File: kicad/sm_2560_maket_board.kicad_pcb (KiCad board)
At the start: 2 copper layers, 81.8 x 61.7 mm, 503 parts

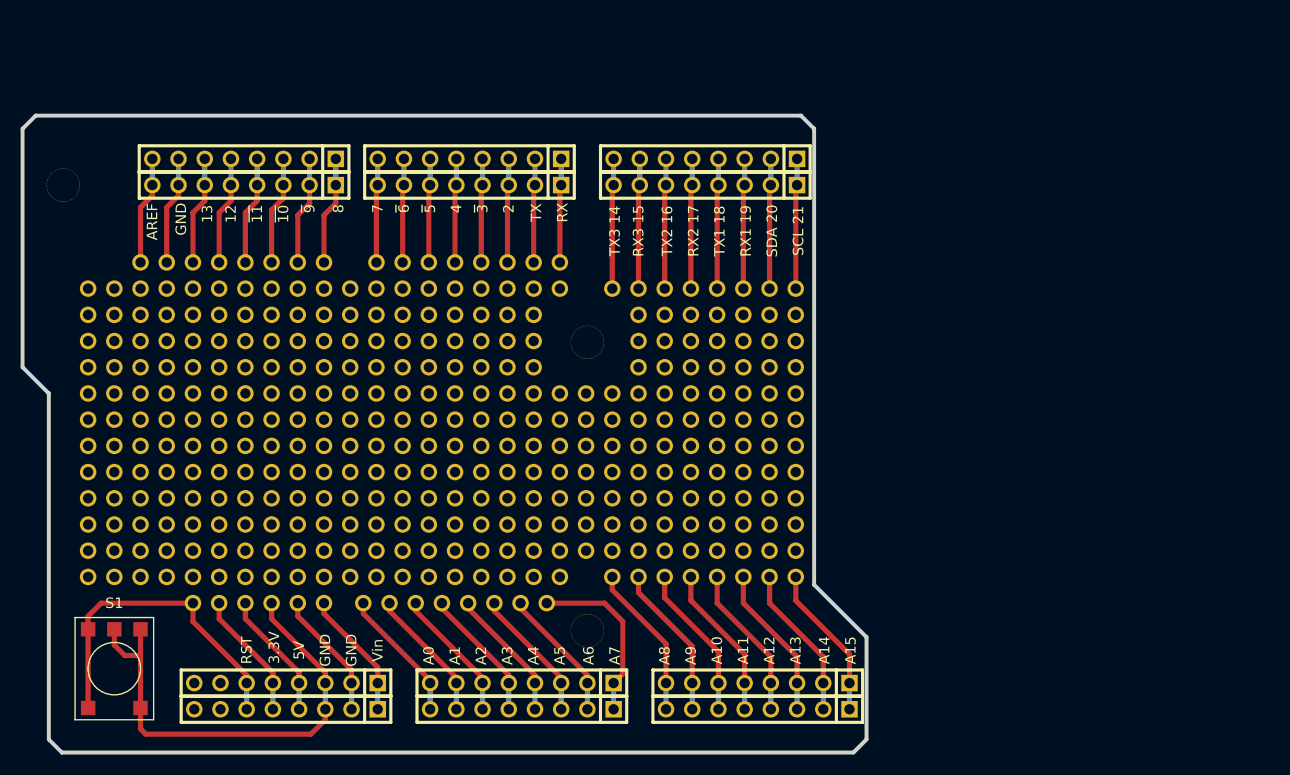
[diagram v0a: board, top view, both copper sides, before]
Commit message: Поправил макетное поле под новую версию платы SafeDuino 2560 ver 2.0.
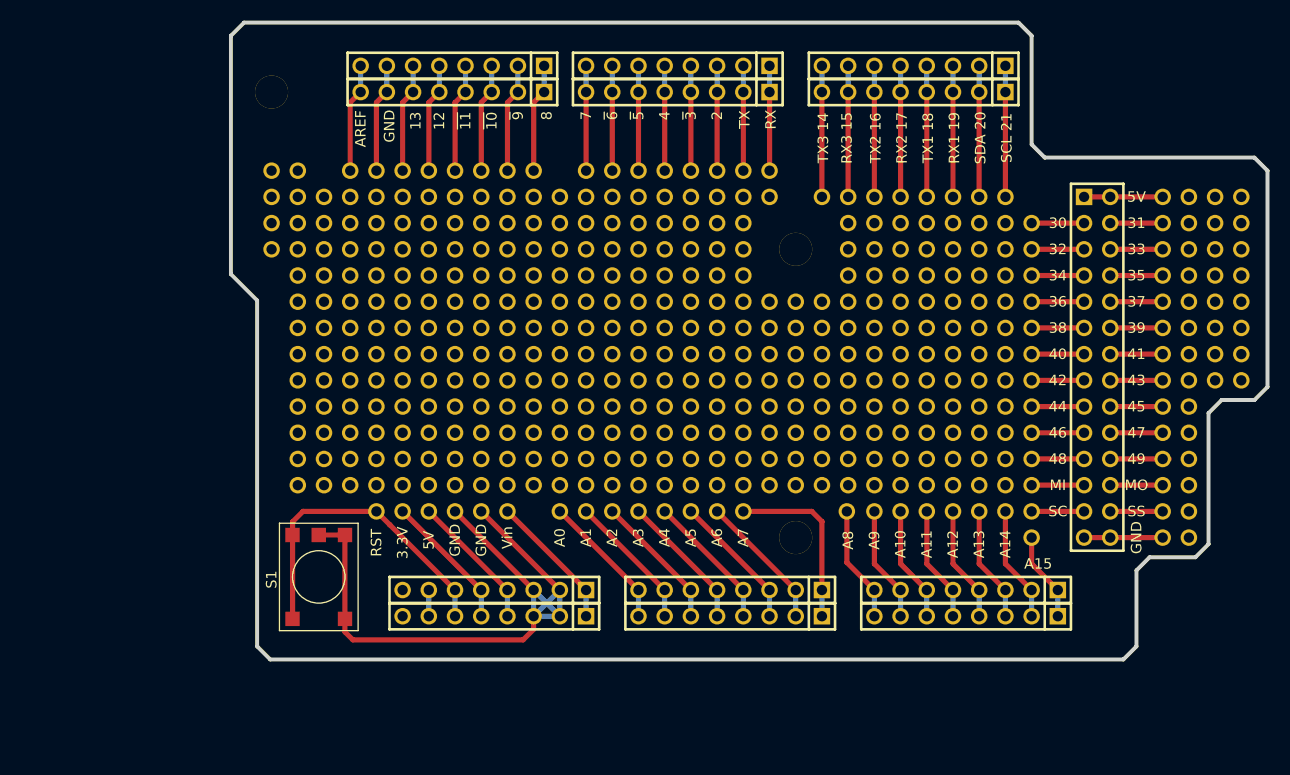
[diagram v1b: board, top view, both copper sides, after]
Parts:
- removed the arduino at (97.9, 136.5)
- removed the arduino at (106.7, 134.6)
- removed the arduino at (83.8, 111.8)
- removed the arduino at (81.7, 112.4)
- removed the arduino at (86.4, 111.8)
- removed the arduino at (94.0, 111.8)
- removed the arduino at (89.3, 112.4)
- removed the arduino at (91.4, 111.8)
- removed the arduino at (88.9, 111.8)
- removed the arduino at (112.1, 112.4)
- removed the arduino at (114.3, 111.8)
- removed the arduino at (111.8, 111.8)
- removed the arduino at (104.5, 135.3)
- removed the arduino at (112.1, 111.1) (x2)
- removed the arduino at (112.1, 108.6) (x2)
- removed the arduino at (111.8, 109.2)
- removed the arduino at (114.3, 109.2)
- removed the arduino at (112.1, 109.9)
- removed the arduino at (88.9, 109.2)
- removed the arduino at (91.4, 109.2)
- removed the arduino at (89.3, 109.9)
- removed the arduino at (94.0, 109.2)
- removed the arduino at (86.4, 109.2)
- removed the arduino at (109.2, 134.6)
- removed the arduino at (81.7, 109.9)
- removed the arduino at (83.8, 109.2)
- removed the arduino at (81.3, 109.2)
- removed the arduino at (96.5, 109.2)
- removed the arduino at (99.1, 109.2)
- removed the arduino at (96.9, 109.9)
- removed the arduino at (101.6, 109.2)
- removed the arduino at (109.2, 109.2)
- removed the arduino at (104.5, 109.9)
- removed the arduino at (106.7, 109.2)
- removed the arduino at (101.6, 134.6)
- removed the arduino at (104.1, 109.2)
- removed the arduino at (79.1, 109.9)
- removed the arduino at (78.7, 109.2)
- removed the arduino at (76.2, 109.2)
- removed the arduino at (71.5, 109.9)
- removed the arduino at (73.7, 109.2)
- removed the arduino at (71.1, 109.2)
- removed the arduino at (71.1, 114.3)
- removed the arduino at (73.7, 114.3)
- removed the arduino at (96.9, 135.3)
- removed the arduino at (71.5, 114.9)
- removed the arduino at (76.2, 114.3)
- removed the arduino at (78.7, 114.3)
- removed the arduino at (79.1, 114.9)
- removed the arduino at (104.1, 114.3)
- removed the arduino at (106.7, 114.3)
- removed the arduino at (104.5, 114.9)
- removed the arduino at (109.2, 114.3)
- removed the arduino at (101.6, 114.3)
- removed the arduino at (96.9, 114.9)
- removed the arduino at (99.1, 134.6)
- removed the arduino at (99.1, 114.3)
- removed the arduino at (96.5, 114.3)
- removed the arduino at (81.3, 114.3)
- removed the arduino at (83.8, 114.3)
- removed the arduino at (81.7, 114.9)
- removed the arduino at (86.4, 114.3)
- removed the arduino at (94.0, 114.3)
- removed the arduino at (89.3, 114.9)
- removed the arduino at (91.4, 114.3)
- removed the arduino at (88.9, 114.3)
- removed the arduino at (96.5, 134.6)
- removed the arduino at (112.1, 114.9)
- removed the arduino at (114.3, 114.3)
- removed the arduino at (111.8, 114.3)
- removed the arduino at (112.1, 113.7)
- removed the arduino at (112.1, 116.2)
- removed the arduino at (134.6, 124.5)
- removed the arduino at (137.2, 124.5)
- removed the arduino at (135.0, 125.1)
- removed the arduino at (139.7, 124.5)
- removed the arduino at (132.1, 124.5)
- removed the arduino at (81.3, 134.6)
- removed the arduino at (127.4, 125.1)
- removed the arduino at (129.5, 124.5)
- removed the arduino at (127.0, 124.5)
- removed the arduino at (111.8, 124.5)
- removed the arduino at (114.3, 124.5)
- removed the arduino at (112.1, 125.1)
- removed the arduino at (116.8, 124.5)
- removed the arduino at (124.5, 124.5)
- removed the arduino at (119.8, 125.1)
- removed the arduino at (121.9, 124.5)
- removed the arduino at (83.8, 134.6)
- removed the arduino at (119.4, 124.5)
- removed the arduino at (88.9, 124.5)
- removed the arduino at (91.4, 124.5)
- removed the arduino at (89.3, 125.1)
- removed the arduino at (94.0, 124.5)
- removed the arduino at (86.4, 124.5)
- removed the arduino at (81.7, 125.1)
- removed the arduino at (83.8, 124.5)
- removed the arduino at (81.3, 124.5)
- removed the arduino at (96.5, 124.5)
- removed the arduino at (81.7, 135.3)
- removed the arduino at (99.1, 124.5)
- removed the arduino at (96.9, 125.1)
- removed the arduino at (101.6, 124.5)
- removed the arduino at (109.2, 124.5)
- removed the arduino at (104.5, 125.1)
- removed the arduino at (106.7, 124.5)
- removed the arduino at (104.1, 124.5)
- removed the arduino at (79.1, 125.1)
- removed the arduino at (78.7, 124.5)
- removed the arduino at (76.2, 124.5)
- removed the arduino at (76.3, 136.5)
- removed the arduino at (86.4, 134.6)
- removed the arduino at (71.5, 125.1)
- removed the arduino at (73.7, 124.5)
- removed the arduino at (71.1, 124.5)
- removed the arduino at (71.1, 121.9)
- removed the arduino at (73.7, 121.9)
- removed the arduino at (71.5, 122.6)
- removed the arduino at (76.2, 121.9)
- removed the arduino at (78.7, 121.9)
- removed the arduino at (79.1, 122.6)
- removed the arduino at (104.1, 121.9)
- removed the arduino at (94.0, 134.6)
- removed the arduino at (106.7, 121.9)
- removed the arduino at (104.5, 122.6)
- removed the arduino at (109.2, 121.9)
- removed the arduino at (101.6, 121.9)
- removed the arduino at (96.9, 122.6)
- removed the arduino at (99.1, 121.9)
- removed the arduino at (96.5, 121.9)
- removed the arduino at (81.3, 121.9)
- removed the arduino at (83.8, 121.9)
- removed the arduino at (81.7, 122.6)
- removed the arduino at (89.3, 135.3)
- removed the arduino at (86.4, 121.9)
- removed the arduino at (94.0, 121.9)
- removed the arduino at (89.3, 122.6)
- removed the arduino at (91.4, 121.9)
- removed the arduino at (88.9, 121.9)
- removed the arduino at (119.4, 121.9)
- removed the arduino at (121.9, 121.9)
- removed the arduino at (119.8, 122.6)
- removed the arduino at (124.5, 121.9)
- removed the arduino at (116.8, 121.9)
- removed the arduino at (91.4, 134.6)
- removed the arduino at (112.1, 122.6)
- removed the arduino at (114.3, 121.9)
- removed the arduino at (111.8, 121.9)
- removed the arduino at (127.0, 121.9)
- removed the arduino at (129.5, 121.9)
- removed the arduino at (127.4, 122.6)
- removed the arduino at (132.1, 121.9)
- removed the arduino at (139.7, 121.9)
- removed the arduino at (135.0, 122.6)
- removed the arduino at (137.2, 121.9)
- removed the arduino at (88.9, 134.6)
- removed the arduino at (134.6, 121.9)
- removed the arduino at (134.6, 116.8)
- removed the arduino at (137.2, 116.8)
- removed the arduino at (135.0, 117.5)
- removed the arduino at (139.7, 116.8)
- removed the arduino at (132.1, 116.8)
- removed the arduino at (127.4, 117.5)
- removed the arduino at (129.5, 116.8)
- removed the arduino at (127.0, 116.8)
- removed the arduino at (111.8, 116.8)
- removed the arduino at (116.8, 134.6)
- removed the arduino at (114.3, 116.8)
- removed the arduino at (112.1, 117.5)
- removed the arduino at (116.8, 116.8)
- removed the arduino at (124.5, 116.8)
- removed the arduino at (119.8, 117.5)
- removed the arduino at (121.9, 116.8)
- removed the arduino at (119.4, 116.8)
- removed the arduino at (88.9, 116.8)
- removed the arduino at (91.4, 116.8)
- removed the arduino at (89.3, 117.5)
- removed the arduino at (112.1, 135.3)
- removed the arduino at (94.0, 116.8)
- removed the arduino at (86.4, 116.8)
- removed the arduino at (81.7, 117.5)
- removed the arduino at (83.8, 116.8)
- removed the arduino at (81.3, 116.8)
- removed the arduino at (96.5, 116.8)
- removed the arduino at (99.1, 116.8)
- removed the arduino at (96.9, 117.5)
- removed the arduino at (101.6, 116.8)
- removed the arduino at (109.2, 116.8)
- removed the arduino at (114.3, 134.6)
- removed the arduino at (104.5, 117.5)
- removed the arduino at (106.7, 116.8)
- removed the arduino at (104.1, 116.8)
- removed the arduino at (79.1, 117.5)
- removed the arduino at (78.7, 116.8)
- removed the arduino at (76.2, 116.8)
- removed the arduino at (71.5, 117.5)
- removed the arduino at (73.7, 116.8)
- removed the arduino at (71.1, 116.8)
- removed the arduino at (71.1, 119.4)
- removed the arduino at (111.8, 134.6)
- removed the arduino at (73.7, 119.4)
- removed the arduino at (71.5, 120.0)
- removed the arduino at (76.2, 119.4)
- removed the arduino at (78.7, 119.4)
- removed the arduino at (79.1, 120.0)
- removed the arduino at (104.1, 119.4)
- removed the arduino at (106.7, 119.4)
- removed the arduino at (104.5, 120.0)
- removed the arduino at (109.2, 119.4)
- removed the arduino at (101.6, 119.4)
- removed the arduino at (116.8, 106.7)
- removed the arduino at (96.9, 120.0)
- removed the arduino at (99.1, 119.4)
- removed the arduino at (96.5, 119.4)
- removed the arduino at (81.3, 119.4)
- removed the arduino at (83.8, 119.4)
- removed the arduino at (81.7, 120.0)
- removed the arduino at (86.4, 119.4)
- removed the arduino at (94.0, 119.4)
- removed the arduino at (89.3, 120.0)
- removed the arduino at (91.4, 119.4)
- removed the arduino at (71.1, 134.6)
- removed the arduino at (112.1, 106.0) (x3)
- removed the arduino at (88.9, 119.4)
- removed the arduino at (119.4, 119.4)
- removed the arduino at (121.9, 119.4)
- removed the arduino at (119.8, 120.0)
- removed the arduino at (124.5, 119.4)
- removed the arduino at (116.8, 119.4)
- removed the arduino at (112.1, 120.0)
- removed the arduino at (114.3, 119.4)
- removed the arduino at (111.8, 119.4)
- removed the arduino at (127.0, 119.4)
- removed the arduino at (71.1, 106.7)
- removed the arduino at (129.5, 119.4)
- removed the arduino at (127.4, 120.0)
- removed the arduino at (132.1, 119.4)
- removed the arduino at (139.7, 119.4)
- removed the arduino at (135.0, 120.0)
- removed the arduino at (137.2, 119.4)
- removed the arduino at (134.6, 119.4)
- removed the arduino at (112.1, 121.3)
- removed the arduino at (134.6, 129.5)
- removed the arduino at (73.7, 106.7)
- removed the arduino at (137.2, 129.5)
- removed the arduino at (135.0, 130.2)
- removed the arduino at (139.7, 129.5)
- removed the arduino at (132.1, 129.5)
- removed the arduino at (127.4, 130.2)
- removed the arduino at (129.5, 129.5)
- removed the arduino at (127.0, 129.5)
- removed the arduino at (111.8, 129.5)
- removed the arduino at (114.3, 129.5)
- removed the arduino at (112.1, 130.2)
- removed the arduino at (71.5, 107.3)
- removed the arduino at (116.8, 129.5)
- removed the arduino at (124.5, 129.5)
- removed the arduino at (119.8, 130.2)
- removed the arduino at (121.9, 129.5)
- removed the arduino at (119.4, 129.5)
- removed the arduino at (88.9, 129.5)
- removed the arduino at (91.4, 129.5)
- removed the arduino at (89.3, 130.2)
- removed the arduino at (94.0, 129.5)
- removed the arduino at (86.4, 129.5)
- removed the arduino at (76.2, 106.7)
- removed the arduino at (81.7, 130.2)
- removed the arduino at (83.8, 129.5)
- removed the arduino at (81.3, 129.5)
- removed the arduino at (96.5, 129.5)
- removed the arduino at (99.1, 129.5)
- removed the arduino at (96.9, 130.2)
- removed the arduino at (101.6, 129.5)
- removed the arduino at (109.2, 129.5)
- removed the arduino at (104.5, 130.2)
- removed the arduino at (106.7, 129.5)
- removed the arduino at (78.7, 106.7)
- removed the arduino at (104.1, 129.5)
- removed the arduino at (79.1, 130.2)
- removed the arduino at (78.7, 129.5)
- removed the arduino at (76.2, 129.5)
- removed the arduino at (71.5, 130.2)
- removed the arduino at (73.7, 129.5)
- removed the arduino at (71.1, 129.5)
- removed the arduino at (71.1, 127.0)
- removed the arduino at (73.7, 127.0)
- removed the arduino at (71.5, 127.6)
- removed the arduino at (79.1, 107.3)
- removed the arduino at (76.2, 127.0)
- removed the arduino at (78.7, 127.0)
- removed the arduino at (79.1, 127.6)
- removed the arduino at (104.1, 127.0)
- removed the arduino at (106.7, 127.0)
- removed the arduino at (104.5, 127.6)
- removed the arduino at (109.2, 127.0)
- removed the arduino at (101.6, 127.0)
- removed the arduino at (96.9, 127.6)
- removed the arduino at (99.1, 127.0)
- removed the arduino at (104.1, 106.7)
- removed the arduino at (96.5, 127.0)
- removed the arduino at (81.3, 127.0)
- removed the arduino at (83.8, 127.0)
- removed the arduino at (81.7, 127.6)
- removed the arduino at (86.4, 127.0)
- removed the arduino at (94.0, 127.0)
- removed the arduino at (89.3, 127.6)
- removed the arduino at (91.4, 127.0)
- removed the arduino at (88.9, 127.0)
- removed the arduino at (119.4, 127.0)
- removed the arduino at (106.7, 106.7)
- removed the arduino at (121.9, 127.0)
- removed the arduino at (119.8, 127.6)
- removed the arduino at (124.5, 127.0)
- removed the arduino at (116.8, 127.0)
- removed the arduino at (112.1, 127.6)
- removed the arduino at (114.3, 127.0)
- removed the arduino at (111.8, 127.0)
- removed the arduino at (127.0, 127.0)
- removed the arduino at (129.5, 127.0)
- removed the arduino at (127.4, 127.6)
- removed the arduino at (104.5, 107.3)
- removed the arduino at (132.1, 127.0)
- removed the arduino at (139.7, 127.0)
- removed the arduino at (135.0, 127.6)
- removed the arduino at (137.2, 127.0)
- removed the arduino at (134.6, 127.0)
- removed the arduino at (134.6, 132.1)
- removed the arduino at (137.2, 132.1)
- removed the arduino at (135.0, 132.7)
- removed the arduino at (139.7, 132.1)
- removed the arduino at (132.1, 132.1)
- removed the arduino at (73.7, 134.6)
- removed the arduino at (109.2, 106.7)
- removed the arduino at (127.4, 132.7)
- removed the arduino at (129.5, 132.1)
- removed the arduino at (127.0, 132.1)
- removed the arduino at (111.8, 132.1)
- removed the arduino at (114.3, 132.1)
- removed the arduino at (112.1, 132.7)
- removed the arduino at (116.8, 132.1)
- removed the arduino at (124.5, 132.1)
- removed the arduino at (119.8, 132.7)
- removed the arduino at (121.9, 132.1)
- removed the arduino at (101.6, 106.7)
- removed the arduino at (119.4, 132.1)
- removed the arduino at (88.9, 132.1)
- removed the arduino at (91.4, 132.1)
- removed the arduino at (89.3, 132.7)
- removed the arduino at (94.0, 132.1)
- removed the arduino at (86.4, 132.1)
- removed the arduino at (81.7, 132.7)
- removed the arduino at (83.8, 132.1)
- removed the arduino at (81.3, 132.1)
- removed the arduino at (96.5, 132.1)
- removed the arduino at (96.9, 107.3)
- removed the arduino at (99.1, 132.1)
- removed the arduino at (96.9, 132.7)
- removed the arduino at (101.6, 132.1)
- removed the arduino at (109.2, 132.1)
- removed the arduino at (104.5, 132.7)
- removed the arduino at (106.7, 132.1)
- removed the arduino at (104.1, 132.1)
- removed the arduino at (79.1, 132.7)
- removed the arduino at (78.7, 132.1)
- removed the arduino at (76.2, 132.1)
- removed the arduino at (99.1, 106.7)
- removed the arduino at (71.5, 132.7)
- removed the arduino at (73.7, 132.1)
- removed the arduino at (71.1, 132.1)
- removed the arduino at (76.2, 104.1)
- removed the arduino at (121.0, 106.0)
- removed the arduino at (139.7, 106.7)
- removed the arduino at (137.2, 106.7)
- removed the arduino at (132.1, 106.7)
- removed the arduino at (134.6, 106.7)
- removed the arduino at (124.5, 106.7)
- removed the arduino at (96.5, 106.7)
- removed the arduino at (121.9, 106.7)
- removed the arduino at (127.0, 106.7)
- removed the arduino at (129.5, 106.7)
- removed the arduino at (106.7, 104.1)
- removed the arduino at (104.1, 104.1)
- removed the arduino at (99.1, 104.1)
- removed the arduino at (101.6, 104.1)
- removed the arduino at (111.8, 104.1)
- removed the arduino at (109.2, 104.1)
- removed the arduino at (114.3, 104.1)
- removed the arduino at (81.3, 106.7)
- removed the arduino at (116.8, 104.1)
- removed the arduino at (98.2, 106.0)
- removed the arduino at (67.7, 118.7)
- removed the arduino at (94.0, 104.1)
- removed the arduino at (91.4, 104.1)
- removed the arduino at (86.4, 104.1)
- removed the arduino at (88.9, 104.1)
- removed the arduino at (78.7, 104.1)
- removed the arduino at (76.6, 106.0)
- removed the arduino at (81.3, 104.1)
- removed the arduino at (83.8, 106.7)
- removed the arduino at (83.8, 104.1)
- removed the arduino at (83.8, 137.2)
- removed the arduino at (81.3, 137.2)
- removed the arduino at (76.3, 134.0)
- removed the arduino at (88.9, 137.2)
- removed the arduino at (86.4, 137.2)
- removed the arduino at (91.4, 137.2)
- removed the arduino at (94.0, 137.2)
- removed the arduino at (75.1, 136.5)
- removed the arduino at (97.9, 134.0)
- removed the arduino at (81.7, 107.3)
- removed the arduino at (115.6, 137.2)
- removed the arduino at (113.0, 137.2)
- removed the arduino at (108.0, 137.2)
- removed the arduino at (110.5, 137.2)
- removed the arduino at (100.3, 137.2)
- removed the arduino at (97.8, 137.2)
- removed the arduino at (102.9, 137.2)
- removed the arduino at (105.4, 137.2)
- removed the arduino at (129.5, 134.6)
- removed the arduino at (127.0, 134.6)
- removed the arduino at (86.4, 106.7)
- removed the arduino at (121.9, 134.6)
- removed the arduino at (124.5, 134.6)
- removed the arduino at (134.6, 134.6)
- removed the arduino at (132.1, 134.6)
- removed the arduino at (137.2, 134.6)
- removed the arduino at (139.8, 134.0)
- removed the arduino at (120.8, 134.0)
- removed the arduino at (112.1, 126.4)
- removed the arduino at (119.8, 133.0)
- removed the arduino at (69.5, 96.6)
- removed the arduino at (94.0, 106.7)
- removed the arduino at (119.5, 139.8)
- removed the arduino at (71.5, 135.3)
- removed the arduino at (89.3, 107.3)
- removed the arduino at (91.4, 106.7)
- removed the arduino at (88.9, 106.7)
- removed the arduino at (112.1, 107.3)
- removed the arduino at (114.3, 106.7)
- removed the arduino at (111.8, 106.7)
- removed the arduino at (134.6, 109.2)
- removed the arduino at (137.2, 109.2)
- removed the arduino at (135.0, 109.9)
- removed the arduino at (76.2, 134.6)
- removed the arduino at (139.7, 109.2)
- removed the arduino at (132.1, 109.2)
- removed the arduino at (127.4, 109.9)
- removed the arduino at (129.5, 109.2)
- removed the arduino at (127.0, 109.2)
- removed the arduino at (124.5, 109.2)
- removed the arduino at (134.6, 114.3)
- removed the arduino at (137.2, 114.3)
- removed the arduino at (135.0, 114.9)
- removed the arduino at (139.7, 114.3)
- removed the arduino at (78.7, 134.6)
- removed the arduino at (132.1, 114.3)
- removed the arduino at (127.4, 114.9)
- removed the arduino at (129.5, 114.3)
- removed the arduino at (127.0, 114.3)
- removed the arduino at (124.5, 114.3)
- removed the arduino at (124.5, 111.8)
- removed the arduino at (127.0, 111.8)
- removed the arduino at (129.5, 111.8)
- removed the arduino at (127.4, 112.4)
- removed the arduino at (132.1, 111.8)
- removed the arduino at (79.1, 135.3)
- removed the arduino at (139.7, 111.8)
- removed the arduino at (135.0, 112.4)
- removed the arduino at (137.2, 111.8)
- removed the arduino at (134.6, 111.8)
- removed the arduino at (71.1, 111.8)
- removed the arduino at (73.7, 111.8)
- removed the arduino at (71.5, 112.4)
- removed the arduino at (76.2, 111.8)
- removed the arduino at (78.7, 111.8)
- removed the arduino at (104.1, 134.6)
- removed the arduino at (79.1, 112.4)
- removed the arduino at (104.1, 111.8)
- removed the arduino at (106.7, 111.8)
- removed the arduino at (104.5, 112.4)
- removed the arduino at (109.2, 111.8)
- removed the arduino at (101.6, 111.8)
- removed the arduino at (96.9, 112.4)
- removed the arduino at (99.1, 111.8)
- removed the arduino at (96.5, 111.8)
- removed the arduino at (81.3, 111.8)
- added XP13: PLD-28, IWconnectors:PIN_ARRAY_14x2, F.Cu at (170.2, 114.3)
- added arduino: P***, 1_pin, F.Cu at (182.9, 97.8)
- added arduino: P***, 1_pin, F.Cu at (182.9, 105.4)
- added arduino: P***, 1_pin, F.Cu at (162.6, 128.3)
- added arduino: P***, 1_pin, F.Cu at (162.6, 118.1)
- added arduino: P***, 1_pin, F.Cu at (160.0, 110.5)
- added arduino: P***, 1_pin, F.Cu at (160.0, 123.2)
- added arduino: P***, 1_pin, F.Cu at (159.0, 112.3)
- added arduino: P***, 1_pin, F.Cu at (160.0, 125.7)
- added arduino: P***, 1_pin, F.Cu at (160.0, 120.7)
- added arduino: P***, 1_pin, F.Cu at (157.5, 118.1)
- added arduino: P***, 1_pin, F.Cu at (157.5, 102.9)
- added arduino: P***, 1_pin, F.Cu at (154.9, 115.6)
- added arduino: P***, 1_pin, F.Cu at (180.3, 105.4)
- added arduino: P***, 1_pin, F.Cu at (157.5, 105.4)
- added arduino: P***, 1_pin, F.Cu at (157.5, 108.0)
- added arduino: P***, 1_pin, F.Cu at (157.5, 100.3)
- added arduino: P***, 1_pin, F.Cu at (154.9, 118.1)
- added arduino: P***, 1_pin, F.Cu at (154.9, 102.9)
- added arduino: P***, 1_pin, F.Cu at (154.9, 113.0)
- added arduino: P***, 1_pin, F.Cu at (154.9, 108.0)
- added arduino: P***, 1_pin, F.Cu at (157.5, 123.2)
- added arduino: P***, 1_pin, F.Cu at (154.9, 100.3)
- added arduino: P***, 1_pin, F.Cu at (157.5, 120.7)
- added arduino: P***, 1_pin, F.Cu at (177.8, 105.4)
- added arduino: P***, 1_pin, F.Cu at (154.9, 105.4)
- added arduino: P***, 1_pin, F.Cu at (157.5, 110.5)
- added arduino: P***, 1_pin, F.Cu at (157.5, 113.0)
- added arduino: P***, 1_pin, F.Cu at (157.5, 125.7)
- added arduino: P***, 1_pin, F.Cu at (157.5, 115.6)
- added arduino: P***, 1_pin, F.Cu at (154.9, 110.5)
- added arduino: P***, 1_pin, F.Cu at (154.9, 123.2)
- added arduino: P***, 1_pin, F.Cu at (153.9, 112.3)
- added arduino: P***, 1_pin, F.Cu at (154.9, 125.7)
- added arduino: P***, 1_pin, F.Cu at (154.9, 120.7)
- added arduino: P***, 1_pin, F.Cu at (182.9, 108.0)
- added arduino: P***, 1_pin, F.Cu at (152.4, 118.1)
- added arduino: P***, 1_pin, F.Cu at (152.4, 102.9)
- added arduino: P***, 1_pin, F.Cu at (149.9, 115.6)
- added arduino: P***, 1_pin, F.Cu at (152.4, 105.4)
- added arduino: P***, 1_pin, F.Cu at (152.4, 108.0)
- added arduino: P***, 1_pin, F.Cu at (152.4, 100.3)
- added arduino: P***, 1_pin, F.Cu at (149.9, 118.1)
- added arduino: P***, 1_pin, F.Cu at (149.9, 102.9)
- added arduino: P***, 1_pin, F.Cu at (149.9, 113.0)
- added arduino: P***, 1_pin, F.Cu at (149.9, 108.0)
- added arduino: P***, 1_pin, F.Cu at (180.3, 108.0)
- added arduino: P***, 1_pin, F.Cu at (152.4, 123.2)
- added arduino: P***, 1_pin, F.Cu at (149.9, 100.3)
- added arduino: P***, 1_pin, F.Cu at (152.4, 120.7)
- added arduino: P***, 1_pin, F.Cu at (149.9, 105.4)
- added arduino: P***, 1_pin, F.Cu at (152.4, 110.5)
- added arduino: P***, 1_pin, F.Cu at (152.4, 113.0)
- added arduino: P***, 1_pin, F.Cu at (152.4, 125.7)
- added arduino: P***, 1_pin, F.Cu at (152.4, 115.6)
- added arduino: P***, 1_pin, F.Cu at (149.9, 110.5)
- added arduino: P***, 1_pin, F.Cu at (149.9, 123.2)
- added arduino: P***, 1_pin, F.Cu at (177.8, 108.0)
- added arduino: P***, 1_pin, F.Cu at (148.8, 112.3)
- added arduino: P***, 1_pin, F.Cu at (149.9, 125.7)
- added arduino: P***, 1_pin, F.Cu at (149.9, 120.7)
- added arduino: P***, 1_pin, F.Cu at (147.3, 118.1)
- added arduino: P***, 1_pin, F.Cu at (147.3, 102.9)
- added arduino: P***, 1_pin, F.Cu at (144.8, 115.6)
- added arduino: P***, 1_pin, F.Cu at (147.3, 105.4)
- added arduino: P***, 1_pin, F.Cu at (147.3, 108.0)
- added arduino: P***, 1_pin, F.Cu at (147.3, 100.3)
- added arduino: P***, 1_pin, F.Cu at (144.8, 118.1)
- added arduino: P***, 1_pin, F.Cu at (182.9, 110.5)
- added arduino: P***, 1_pin, F.Cu at (144.8, 102.9)
- added arduino: P***, 1_pin, F.Cu at (144.8, 113.0)
- added arduino: P***, 1_pin, F.Cu at (144.8, 108.0)
- added arduino: P***, 1_pin, F.Cu at (147.3, 123.2)
- added arduino: P***, 1_pin, F.Cu at (144.8, 100.3)
- added arduino: P***, 1_pin, F.Cu at (147.3, 120.7)
- added arduino: P***, 1_pin, F.Cu at (144.8, 105.4)
- added arduino: P***, 1_pin, F.Cu at (147.3, 110.5)
- added arduino: P***, 1_pin, F.Cu at (147.3, 113.0)
- added arduino: P***, 1_pin, F.Cu at (147.3, 125.7)
- added arduino: P***, 1_pin, F.Cu at (180.3, 110.5)
- added arduino: P***, 1_pin, F.Cu at (147.3, 115.6)
- added arduino: P***, 1_pin, F.Cu at (144.8, 110.5)
- added arduino: P***, 1_pin, F.Cu at (144.8, 123.2)
- added arduino: P***, 1_pin, F.Cu at (143.8, 112.3)
- added arduino: P***, 1_pin, F.Cu at (144.8, 125.7)
- added arduino: P***, 1_pin, F.Cu at (144.8, 120.7)
- added arduino: P***, 1_pin, F.Cu at (134.6, 115.6)
- added arduino: P***, 1_pin, F.Cu at (134.6, 100.3)
- added arduino: P***, 1_pin, F.Cu at (132.1, 113.0)
- added arduino: P***, 1_pin, F.Cu at (134.6, 102.9)
- added arduino: P***, 1_pin, F.Cu at (177.8, 110.5)
- added arduino: P***, 1_pin, F.Cu at (134.6, 105.4)
- added arduino: P***, 1_pin, F.Cu at (134.6, 97.8)
- added arduino: P***, 1_pin, F.Cu at (132.1, 115.6)
- added arduino: P***, 1_pin, F.Cu at (132.1, 100.3)
- added arduino: P***, 1_pin, F.Cu at (132.1, 110.5)
- added arduino: P***, 1_pin, F.Cu at (132.1, 105.4)
- added arduino: P***, 1_pin, F.Cu at (134.6, 120.7)
- added arduino: P***, 1_pin, F.Cu at (132.1, 97.8)
- added arduino: P***, 1_pin, F.Cu at (134.6, 118.1)
- added arduino: P***, 1_pin, F.Cu at (132.1, 102.9)
- added arduino: P***, 1_pin, F.Cu at (182.9, 113.0)
- added arduino: P***, 1_pin, F.Cu at (134.6, 108.0)
- added arduino: P***, 1_pin, F.Cu at (134.6, 110.5)
- added arduino: P***, 1_pin, F.Cu at (134.6, 123.2)
- added arduino: P***, 1_pin, F.Cu at (134.6, 113.0)
- added arduino: P***, 1_pin, F.Cu at (132.1, 108.0)
- added arduino: P***, 1_pin, F.Cu at (132.1, 120.7)
- added arduino: P***, 1_pin, F.Cu at (131.1, 109.7)
- added arduino: P***, 1_pin, F.Cu at (132.1, 123.2)
- added arduino: P***, 1_pin, F.Cu at (132.1, 118.1)
- added arduino: P***, 1_pin, F.Cu at (129.5, 115.6)
- added arduino: P***, 1_pin, F.Cu at (180.3, 97.8)
- added arduino: P***, 1_pin, F.Cu at (180.3, 113.0)
- added arduino: P***, 1_pin, F.Cu at (129.5, 100.3)
- added arduino: P***, 1_pin, F.Cu at (127.0, 113.0)
- added arduino: P***, 1_pin, F.Cu at (129.5, 102.9)
- added arduino: P***, 1_pin, F.Cu at (129.5, 105.4)
- added arduino: P***, 1_pin, F.Cu at (129.5, 97.8)
- added arduino: P***, 1_pin, F.Cu at (127.0, 115.6)
- added arduino: P***, 1_pin, F.Cu at (127.0, 100.3)
- added arduino: P***, 1_pin, F.Cu at (127.0, 110.5)
- added arduino: P***, 1_pin, F.Cu at (127.0, 105.4)
- added arduino: P***, 1_pin, F.Cu at (129.5, 120.7)
- added arduino: P***, 1_pin, F.Cu at (177.8, 113.0)
- added arduino: P***, 1_pin, F.Cu at (127.0, 97.8)
- added arduino: P***, 1_pin, F.Cu at (129.5, 118.1)
- added arduino: P***, 1_pin, F.Cu at (127.0, 102.9)
- added arduino: P***, 1_pin, F.Cu at (129.5, 108.0)
- added arduino: P***, 1_pin, F.Cu at (129.5, 110.5)
- added arduino: P***, 1_pin, F.Cu at (129.5, 123.2)
- added arduino: P***, 1_pin, F.Cu at (129.5, 113.0)
- added arduino: P***, 1_pin, F.Cu at (127.0, 108.0)
- added arduino: P***, 1_pin, F.Cu at (127.0, 120.7)
- added arduino: P***, 1_pin, F.Cu at (126.0, 109.7)
- added arduino: P***, 1_pin, F.Cu at (182.9, 115.6)
- added arduino: P***, 1_pin, F.Cu at (127.0, 123.2)
- added arduino: P***, 1_pin, F.Cu at (127.0, 118.1)
- added arduino: P***, 1_pin, F.Cu at (124.5, 115.6)
- added arduino: P***, 1_pin, F.Cu at (124.5, 100.3)
- added arduino: P***, 1_pin, F.Cu at (121.9, 113.0)
- added arduino: P***, 1_pin, F.Cu at (124.5, 102.9)
- added arduino: P***, 1_pin, F.Cu at (124.5, 105.4)
- added arduino: P***, 1_pin, F.Cu at (124.5, 97.8)
- added arduino: P***, 1_pin, F.Cu at (121.9, 115.6)
- added arduino: P***, 1_pin, F.Cu at (121.9, 100.3)
- added arduino: P***, 1_pin, F.Cu at (180.3, 115.6)
- added arduino: P***, 1_pin, F.Cu at (121.9, 110.5)
- added arduino: P***, 1_pin, F.Cu at (121.9, 105.4)
- added arduino: P***, 1_pin, F.Cu at (124.5, 120.7)
- added arduino: P***, 1_pin, F.Cu at (121.9, 97.8)
- added arduino: P***, 1_pin, F.Cu at (124.5, 118.1)
- added arduino: P***, 1_pin, F.Cu at (121.9, 102.9)
- added arduino: P***, 1_pin, F.Cu at (124.5, 108.0)
- added arduino: P***, 1_pin, F.Cu at (124.5, 110.5)
- added arduino: P***, 1_pin, F.Cu at (124.5, 123.2)
- added arduino: P***, 1_pin, F.Cu at (124.5, 113.0)
- added arduino: P***, 1_pin, F.Cu at (177.8, 115.6)
- added arduino: P***, 1_pin, F.Cu at (121.9, 108.0)
- added arduino: P***, 1_pin, F.Cu at (121.9, 120.7)
- added arduino: P***, 1_pin, F.Cu at (120.9, 109.7)
- added arduino: P***, 1_pin, F.Cu at (121.9, 123.2)
- added arduino: P***, 1_pin, F.Cu at (121.9, 118.1)
- added arduino: P***, 1_pin, F.Cu at (119.4, 115.6)
- added arduino: P***, 1_pin, F.Cu at (119.4, 100.3)
- added arduino: P***, 1_pin, F.Cu at (116.8, 113.0)
- added arduino: P***, 1_pin, F.Cu at (119.4, 102.9)
- added arduino: P***, 1_pin, F.Cu at (119.4, 105.4)
- added arduino: P***, 1_pin, F.Cu at (177.8, 118.1)
- added arduino: P***, 1_pin, F.Cu at (119.4, 97.8)
- added arduino: P***, 1_pin, F.Cu at (116.8, 115.6)
- added arduino: P***, 1_pin, F.Cu at (116.8, 100.3)
- added arduino: P***, 1_pin, F.Cu at (116.8, 110.5)
- added arduino: P***, 1_pin, F.Cu at (116.8, 105.4)
- added arduino: P***, 1_pin, F.Cu at (119.4, 120.7)
- added arduino: P***, 1_pin, F.Cu at (116.8, 97.8)
- added arduino: P***, 1_pin, F.Cu at (119.4, 118.1)
- added arduino: P***, 1_pin, F.Cu at (116.8, 102.9)
- added arduino: P***, 1_pin, F.Cu at (119.4, 108.0)
- added arduino: P***, 1_pin, F.Cu at (177.8, 120.7)
- added arduino: P***, 1_pin, F.Cu at (119.4, 110.5)
- added arduino: P***, 1_pin, F.Cu at (119.4, 123.2)
- added arduino: P***, 1_pin, F.Cu at (119.4, 113.0)
- added arduino: P***, 1_pin, F.Cu at (116.8, 108.0)
- added arduino: P***, 1_pin, F.Cu at (116.8, 120.7)
- added arduino: P***, 1_pin, F.Cu at (115.8, 109.7)
- added arduino: P***, 1_pin, F.Cu at (116.8, 123.2)
- added arduino: P***, 1_pin, F.Cu at (116.8, 118.1)
- added arduino: P***, 1_pin, F.Cu at (114.3, 115.6)
- added arduino: P***, 1_pin, F.Cu at (114.3, 100.3)
- added arduino: P***, 1_pin, F.Cu at (177.8, 123.2)
- added arduino: P***, 1_pin, F.Cu at (111.8, 113.0)
- added arduino: P***, 1_pin, F.Cu at (114.3, 102.9)
- added arduino: P***, 1_pin, F.Cu at (114.3, 105.4)
- added arduino: P***, 1_pin, F.Cu at (114.3, 97.8)
- added arduino: P***, 1_pin, F.Cu at (111.8, 115.6)
- added arduino: P***, 1_pin, F.Cu at (111.8, 100.3)
- added arduino: P***, 1_pin, F.Cu at (111.8, 110.5)
- added arduino: P***, 1_pin, F.Cu at (111.8, 105.4)
- added arduino: P***, 1_pin, F.Cu at (114.3, 120.7)
- added arduino: P***, 1_pin, F.Cu at (111.8, 97.8)
- added arduino: P***, 1_pin, F.Cu at (177.8, 125.7)
- added arduino: P***, 1_pin, F.Cu at (114.3, 118.1)
- added arduino: P***, 1_pin, F.Cu at (111.8, 102.9)
- added arduino: P***, 1_pin, F.Cu at (114.3, 108.0)
- added arduino: P***, 1_pin, F.Cu at (114.3, 110.5)
- added arduino: P***, 1_pin, F.Cu at (114.3, 123.2)
- added arduino: P***, 1_pin, F.Cu at (114.3, 113.0)
- added arduino: P***, 1_pin, F.Cu at (111.8, 108.0)
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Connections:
- XP7 pad 7: (no net) -> /IOREF
- XP7 pad 8: (no net) -> Net-(XP7-Pad8)
- XP8 pad 7: (no net) -> /IOREF
- XP8 pad 8: (no net) -> Net-(XP8-Pad8)
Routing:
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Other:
- board size 81.8 x 61.7 mm -> 100.5 x 61.7 mm
- board text added: "30"
- board text added: "31"
- board text added: "32"
- board text added: "33"
- board text added: "34"
- board text added: "35"
- board text added: "36"
- board text added: "37"
- board text added: "38"
- board text added: "39"
- board text added: "40"
- board text added: "41"
- board text added: "42"
- board text added: "43"
- board text added: "44"
- board text added: "45"
- board text added: "46"
- board text added: "47"
- board text added: "48"
- board text added: "49"
- board text added: "MI"
- board text added: "MO"
- board text added: "SC"
- board text added: "SS"

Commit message: Перевёл проект на новую версию kicad.
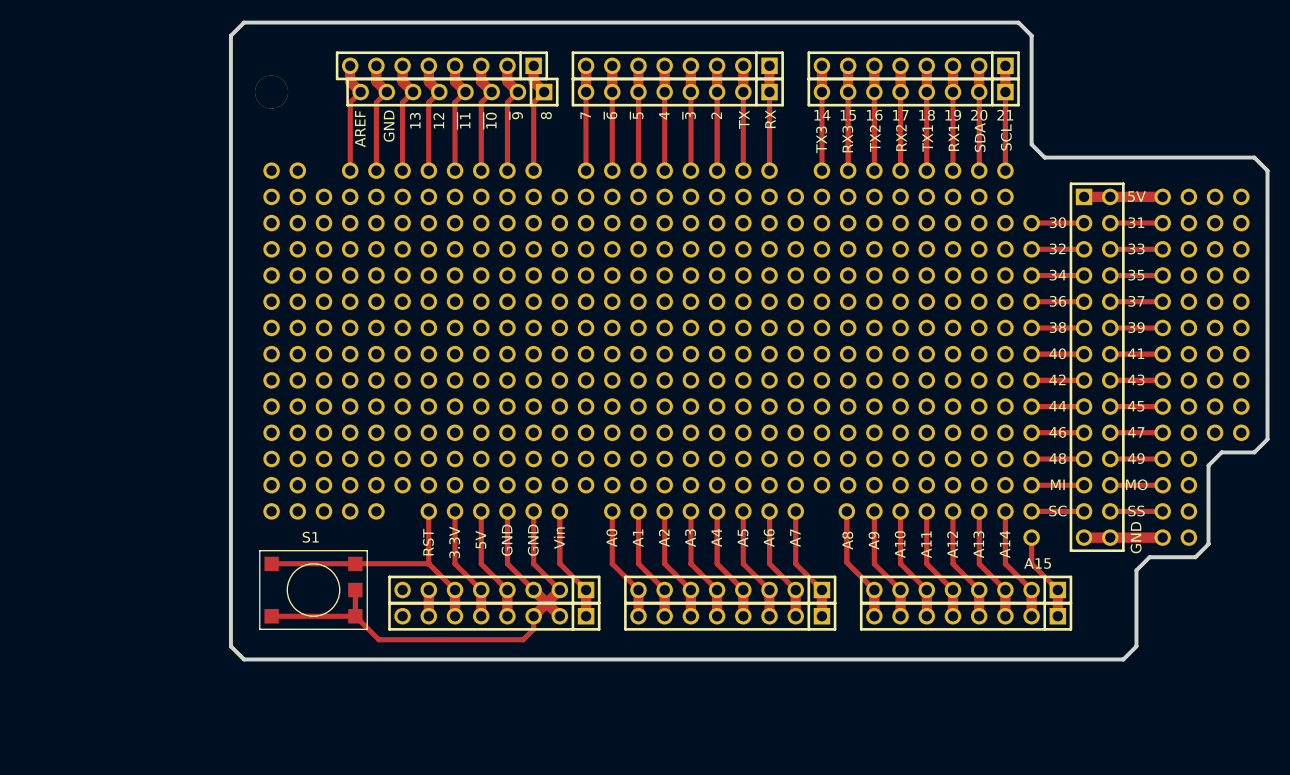
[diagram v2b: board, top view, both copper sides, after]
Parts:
- removed the arduino at (140.0, 124.0)
- removed the arduino at (139.7, 130.8)
- added arduino: P***, 1_pin, F.Cu at (88.9, 120.7)
- added arduino: P***, 1_pin, F.Cu at (88.9, 128.3)
- added arduino: P***, 1_pin, F.Cu at (154.9, 97.8)
- added arduino: P***, 1_pin, F.Cu at (139.7, 105.4)
- added arduino: P***, 1_pin, F.Cu at (137.2, 102.9)
- added arduino: P***, 1_pin, F.Cu at (88.9, 110.5)
- added arduino: P***, 1_pin, F.Cu at (142.2, 102.9)
- added arduino: P***, 1_pin, F.Cu at (147.3, 97.8)
- added arduino: P***, 1_pin, F.Cu at (88.9, 115.6)
- added arduino: P***, 1_pin, F.Cu at (88.9, 123.2)
- added arduino: P***, 1_pin, F.Cu at (149.9, 97.8)
- added arduino: P***, 1_pin, F.Cu at (94.0, 128.3)
- added arduino: P***, 1_pin, F.Cu at (157.5, 97.8)
- added arduino: P***, 1_pin, F.Cu at (139.7, 100.3)
- added arduino: P***, 1_pin, F.Cu at (139.7, 97.8)
- added arduino: P***, 1_pin, F.Cu at (142.2, 100.3)
- added arduino: P***, 1_pin, F.Cu at (139.7, 102.9)
- added arduino: P***, 1_pin, F.Cu at (88.9, 113.0)
- added arduino: P***, 1_pin, F.Cu at (142.2, 97.8)
- added arduino: P***, 1_pin, F.Cu at (152.4, 97.8)
- added arduino: P***, 1_pin, F.Cu at (88.9, 118.1)
- added arduino: P***, 1_pin, F.Cu at (88.9, 125.7)
- added arduino: P***, 1_pin, F.Cu at (137.2, 105.4)
- added arduino: P***, 1_pin, F.Cu at (144.8, 97.8)
- added arduino: P***, 1_pin, F.Cu at (137.2, 100.3)
- added arduino: P***, 1_pin, F.Cu at (182.9, 120.7)
- added arduino: P***, 1_pin, F.Cu at (180.3, 120.7)
- added arduino: P***, 1_pin, F.Cu at (99.1, 128.3)
- added arduino: P***, 1_pin, F.Cu at (91.4, 128.3)
- added arduino: P***, 1_pin, F.Cu at (88.9, 105.4)
- added arduino: P***, 1_pin, F.Cu at (96.5, 128.3)
- added arduino: P***, 1_pin, F.Cu at (160.0, 97.8)
- added arduino: P***, 1_pin, F.Cu at (88.9, 108.0)
- added arduino: P***, 1_pin, F.Cu at (180.3, 118.1)
- added arduino: P***, 1_pin, F.Cu at (182.9, 118.1)
- added arduino: P***, 1_pin, F.Cu at (142.2, 105.4)
- moved arduino 5.08 mm to (106.7, 128.3)
- moved arduino 5.08 mm to (134.6, 128.3)
- moved arduino 5.08 mm to (132.1, 128.3)
- moved arduino 5.08 mm to (124.5, 128.3)
- moved arduino 5.08 mm to (129.5, 128.3)
- moved arduino 5.08 mm to (127.0, 128.3)
- moved arduino 5.08 mm to (121.9, 128.3)
- moved arduino 5.08 mm to (114.3, 128.3)
- moved arduino 5.08 mm to (116.8, 128.3)
- moved arduino 5.08 mm to (109.2, 128.3)
- moved arduino 5.08 mm to (111.8, 128.3)
- moved arduino 5.08 mm to (104.1, 128.3)
- moved arduino 5.08 mm to (137.2, 128.3)
- moved arduino 5.08 mm to (139.7, 128.3)
- moved arduino 2.54 mm to (149.9, 95.2)
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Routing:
- net /GND: track 86.8 -> 73.7 mm
- net /ADC7: track 17.2 -> 11.2 mm
- net /RESET: track 31.3 -> 26.5 mm
- net /PD1: track 12.7 -> 10.2 mm
- net /PH1: track 12.7 -> 10.2 mm
- net /PJ0: track 12.7 -> 10.2 mm
- net /PH0: track 12.7 -> 10.2 mm
- net /PD3: track 12.7 -> 10.2 mm
- net /PD2: track 12.7 -> 10.2 mm
- net /PD0: track 12.7 -> 10.2 mm
- net /PJ1: track 12.7 -> 10.2 mm
- net /VCC3V3: track 13.3 -> 11.2 mm
- net /ADC5: track 13.3 -> 11.2 mm
- net /ADC4: track 13.3 -> 11.2 mm
- net /MPU_VCC: track 20.9 -> 18.8 mm
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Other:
- outline, holes or cut-outs redrawn
- net class Default removed
- board text added: "14"
- board text added: "15"
- board text added: "16"
- board text added: "17"
- board text added: "18"
- board text added: "19"
- board text added: "20"
- board text added: "21"
- board text added: "RX1"
- board text added: "RX2"
- board text added: "RX3"
- board text added: "SCL"
- board text added: "SDA"
- board text added: "TX1"
- board text added: "TX2"
- board text added: "TX3"
- board text added: "~{10}"
- board text added: "~{11}"
- board text added: "~{3}"
- board text added: "~{5}"
- board text added: "~{6}"
- board text added: "~{9}"
- board text removed: "RX1 19"
- board text removed: "RX2 17"
- board text removed: "RX3 15"
- board text removed: "SCL 21"
- board text removed: "SDA 20"
- board text removed: "TX1 18"
- board text removed: "TX2 16"
- board text removed: "TX3 14"
- board text removed: "~10"
- board text removed: "~11"
- board text removed: "~3"
- board text removed: "~5"
- board text removed: "~6"
- board text removed: "~9"
